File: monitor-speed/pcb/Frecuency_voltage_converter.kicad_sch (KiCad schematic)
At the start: 19 parts, among them U3 4070, U4 TL082

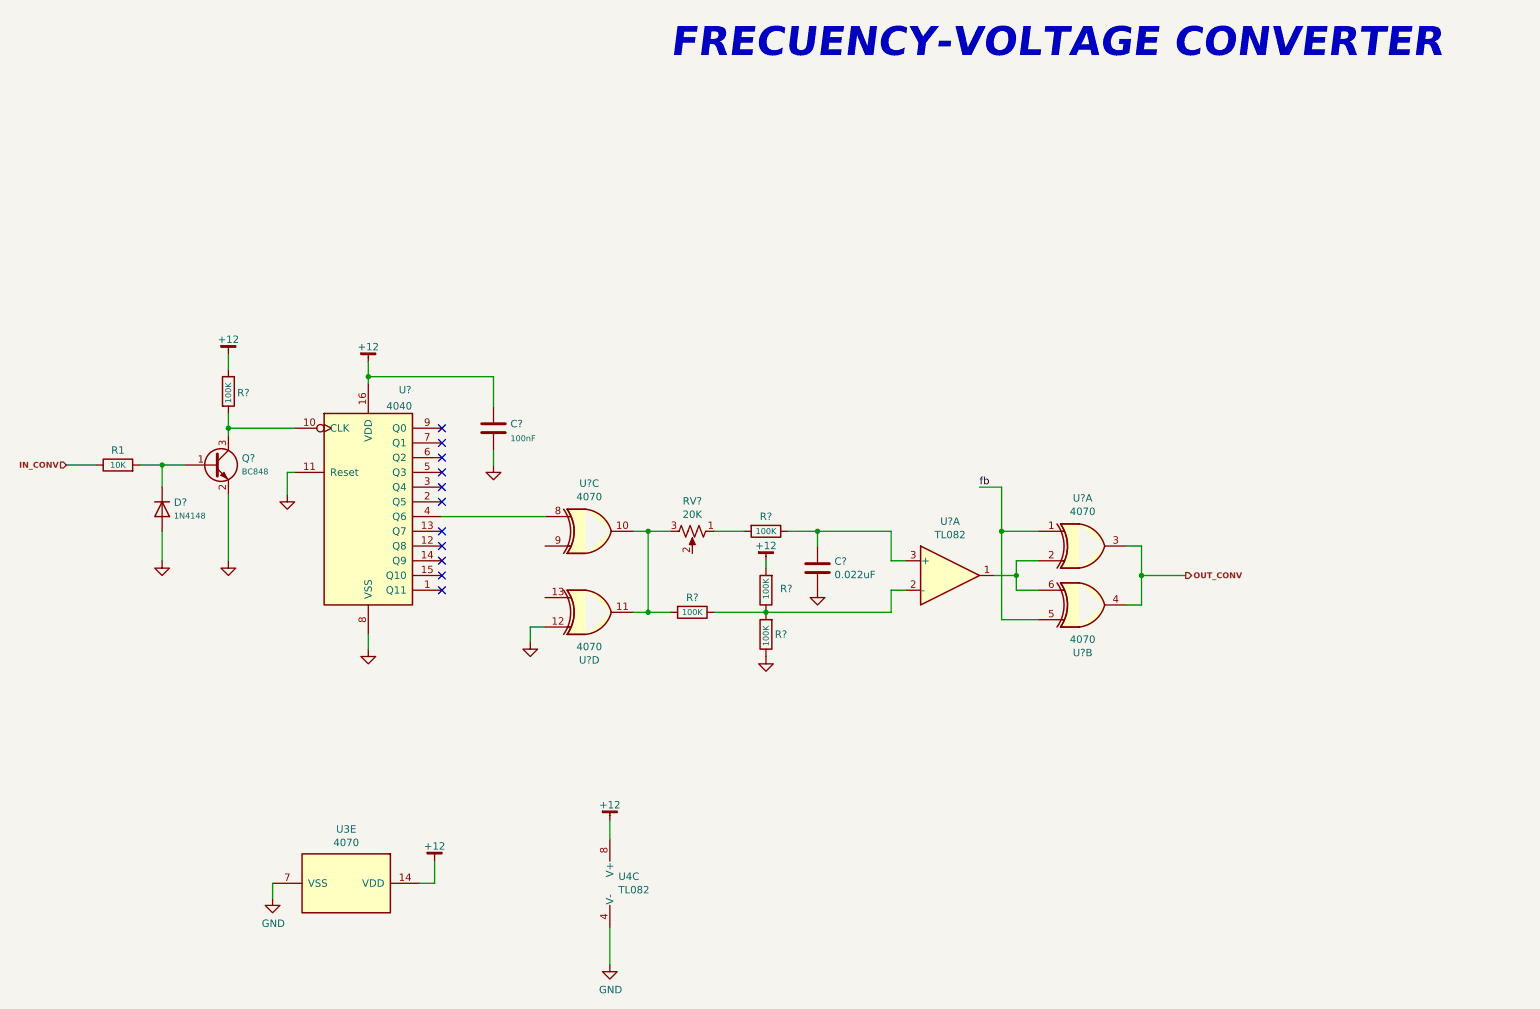
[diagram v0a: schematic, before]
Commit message: Monitor-Speed: New Schematic
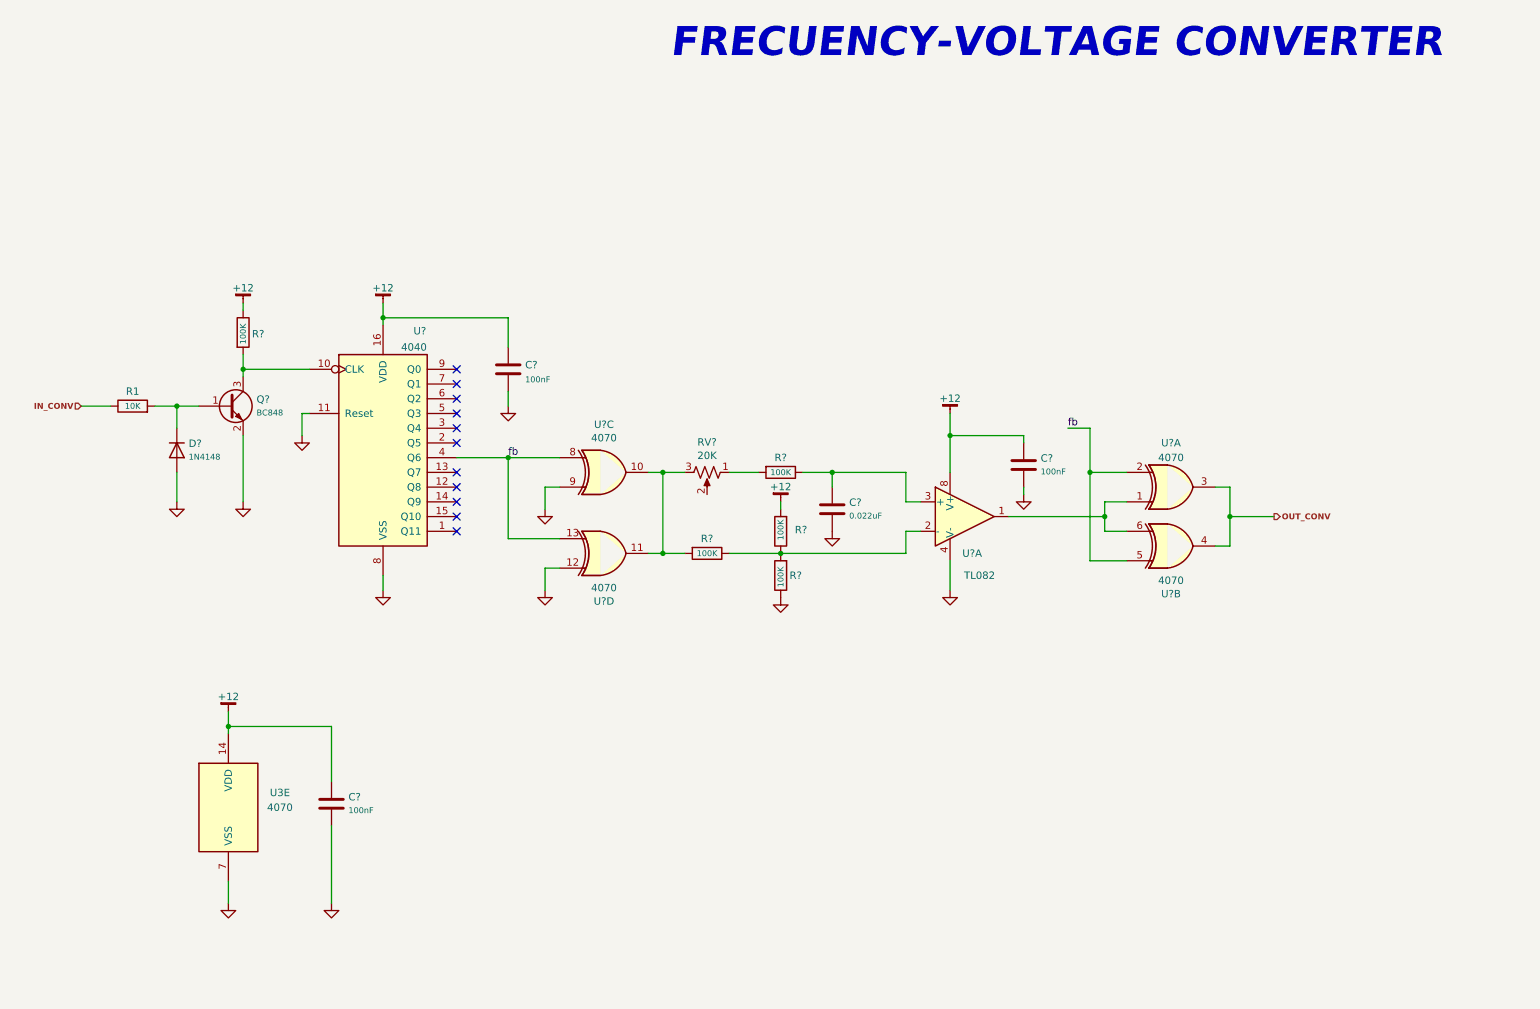
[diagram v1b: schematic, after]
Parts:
- removed U4, U?: TL082, Package_SO:SOIC-8-1EP_3.9x4.9mm_P1.27mm_EP2.29x3mm, symbol Amplifier_Operational:TL082
- added C? (x2): 100nF, Capacitor_SMD:C_0603_1608Metric_Pad1.08x0.95mm_HandSolder, symbol Device:C
- added U? (x2): TL082, symbol Amplifier_Operational:TL082
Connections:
- net +12: now also C?.1, C?.1, U?.8 (V+)
- net GND: now also U?.9, C?.2, C?.2, U?.4 (V-)
- net fb: now also U?.13, U?.2, U?.4 (Q6), U?.8; no longer U?.1
- net at C?.1, R?.1: now also U?.3 (+)
- net at U?.6: now also U?.1, U?.1; no longer U?.2
- net at R?.1, R?.1, R?.2: now also U?.2 (-)
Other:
- moved on the sheet: C?, D?, Q?, R1, R?, RV?, U3E, U?, U?A, U?B, U?C, U?D

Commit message: Monitor-Speed: Add Relay Circuit
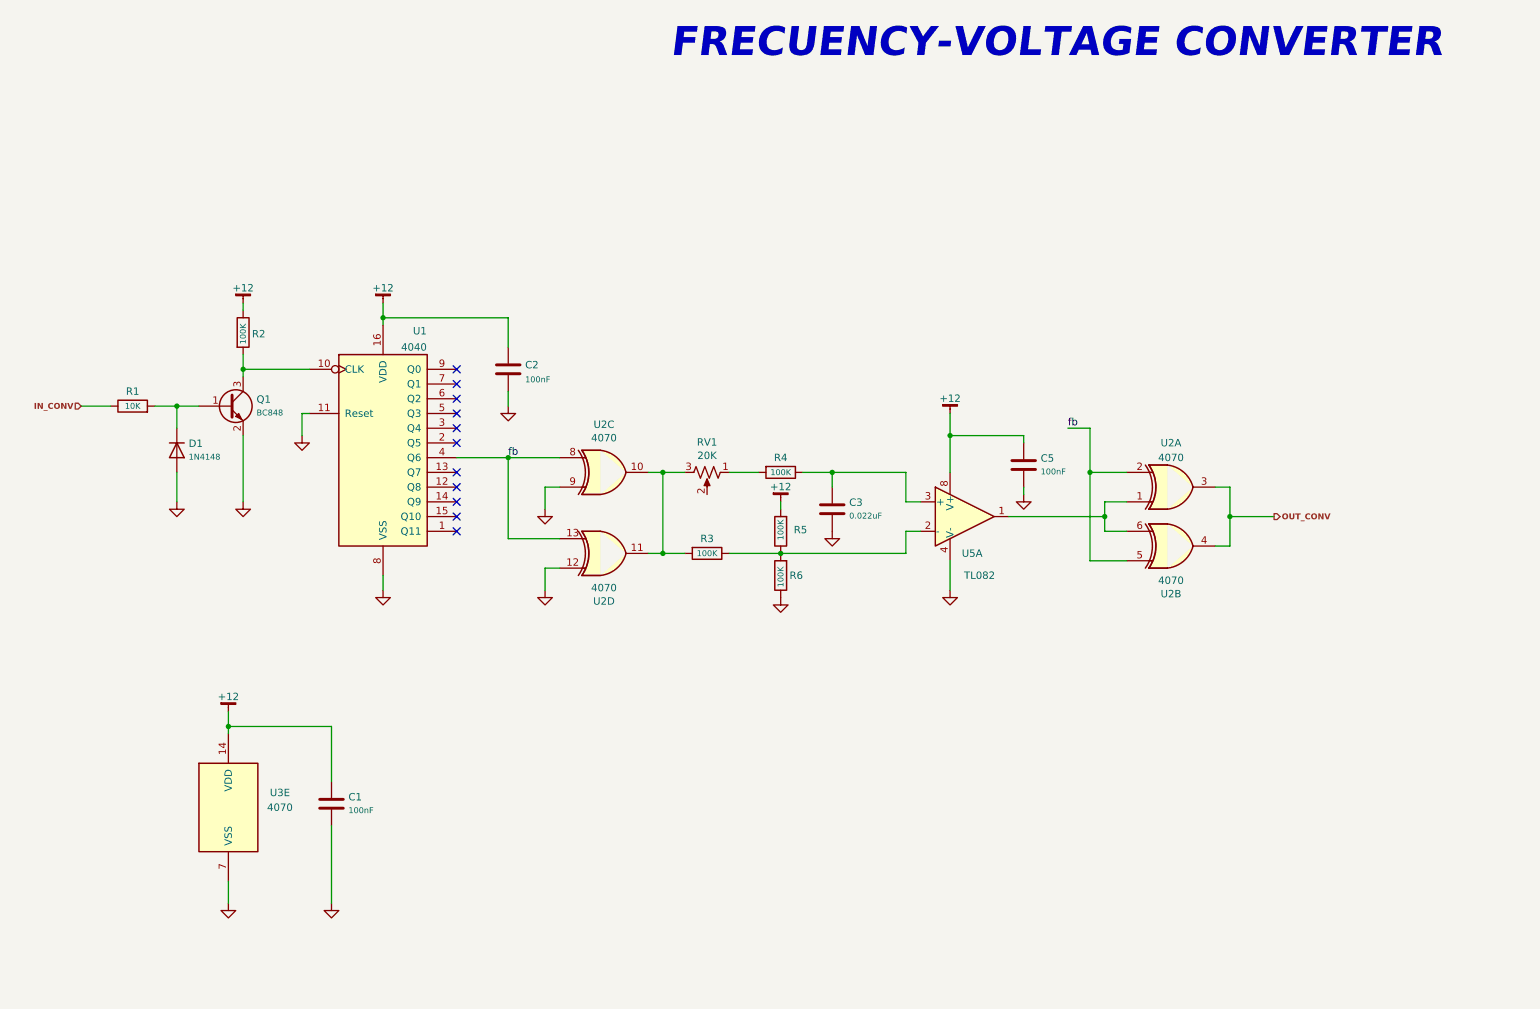
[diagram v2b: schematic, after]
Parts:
- gave numbers to parts that had none: 15
